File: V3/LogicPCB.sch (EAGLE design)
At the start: 58 parts, among them CON1 CUBE_ORANGE_, CON13 CON-6P-JST-XA, CON14 PINHEAD_1X04-2.54, CON15 CON-4P-JST-XA, CON17 CON-4P-JST-XA, CON18 CON-6P-JST-XA, CON19 USB-TYPE-C-VERT-PROD, CON2 CON-4P-JST-XA, CON20 PINHEAD_1X06-2.54, CON21 CON-4P-JST-XA, CON22 CON-4P-JST-XA, CON23 CON-4P-JST-XA, CON24 CON-4P-JST-XA, CON25 CON-4P-JST-XA, CON26 CON-4P-JST-XA, CON27 CON-4P-JST-XA, CON28 CON-4P-JST-XA, CON29 CON-4P-JST-XA, CON3 PINHEAD_1X08-2.54, CON30 CON-4P-JST-XA, CON32 CON-4P-JST-XA, CON35 CON-12P-JST-XA, CON4 CON-2P-JST-XA, CON5 CON-6P-JST-XA, CON6 CON-4P-JST-XA, CON7 PINHEAD_1X06-2.54, CON8 PINHEAD_1X08-2.54, IC2 AOZ1280, M1 05G_ETHERNET_SWITCH, Q1 IRLML0030

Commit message: updates for V3
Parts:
- removed CON3: PINHEAD_1X08-2.54, pinhead:PINHEAD_1X08-2.54
- added CON9: PINHEAD_1X12-2.54, pinhead:PINHEAD_1X12-2.54
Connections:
- net CAM_RX+ renamed ETH3_TX+
- net CAM_TX+ renamed ETH3_RX+
- net CAM_TX- renamed ETH3_RX-
- net CAN_RX- renamed ETH3_TX-
- net N$10 renamed ETH1_TX+
- net N$11 renamed ETH1_TX-
- net N$12 renamed ETH1_RX+
- net N$17 renamed ETH1_RX-
- net PL_ETH_RX+ renamed ETH5_TX-
- net PL_ETH_RX- renamed ETH5_TX+
- net PL_ETH_TX+ renamed ETH5_RX-
- net PL_ETH_TX- renamed ETH5_RX+
- net 5VFMU: now also CON9.6, CON9.7, CON9.8; no longer CON3.6, CON3.7, CON3.8
- net BATT_CURRENT: now also CON9.1; no longer CON3.1
- net BATT_VOLTAGE: now also CON9.2; no longer CON3.2
- net GND: now also CON35.10, CON9.11, CON9.12, CON9.3, CON9.4, CON9.5; no longer CON3.3, CON3.4, CON3.5
- net SERIAL3_RX: now also CON35.6; no longer CON35.8
- net SERIAL3_TX: now also CON35.5; no longer CON35.7
- net VDD_24V: now also CON35.7, CON35.8; no longer CON35.10
- net VDD_4V: now also CON9.10, CON9.9
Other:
- moved on the sheet: CON13, CON21, CON35, M1G$1, M1J1, M1J3, M1J5

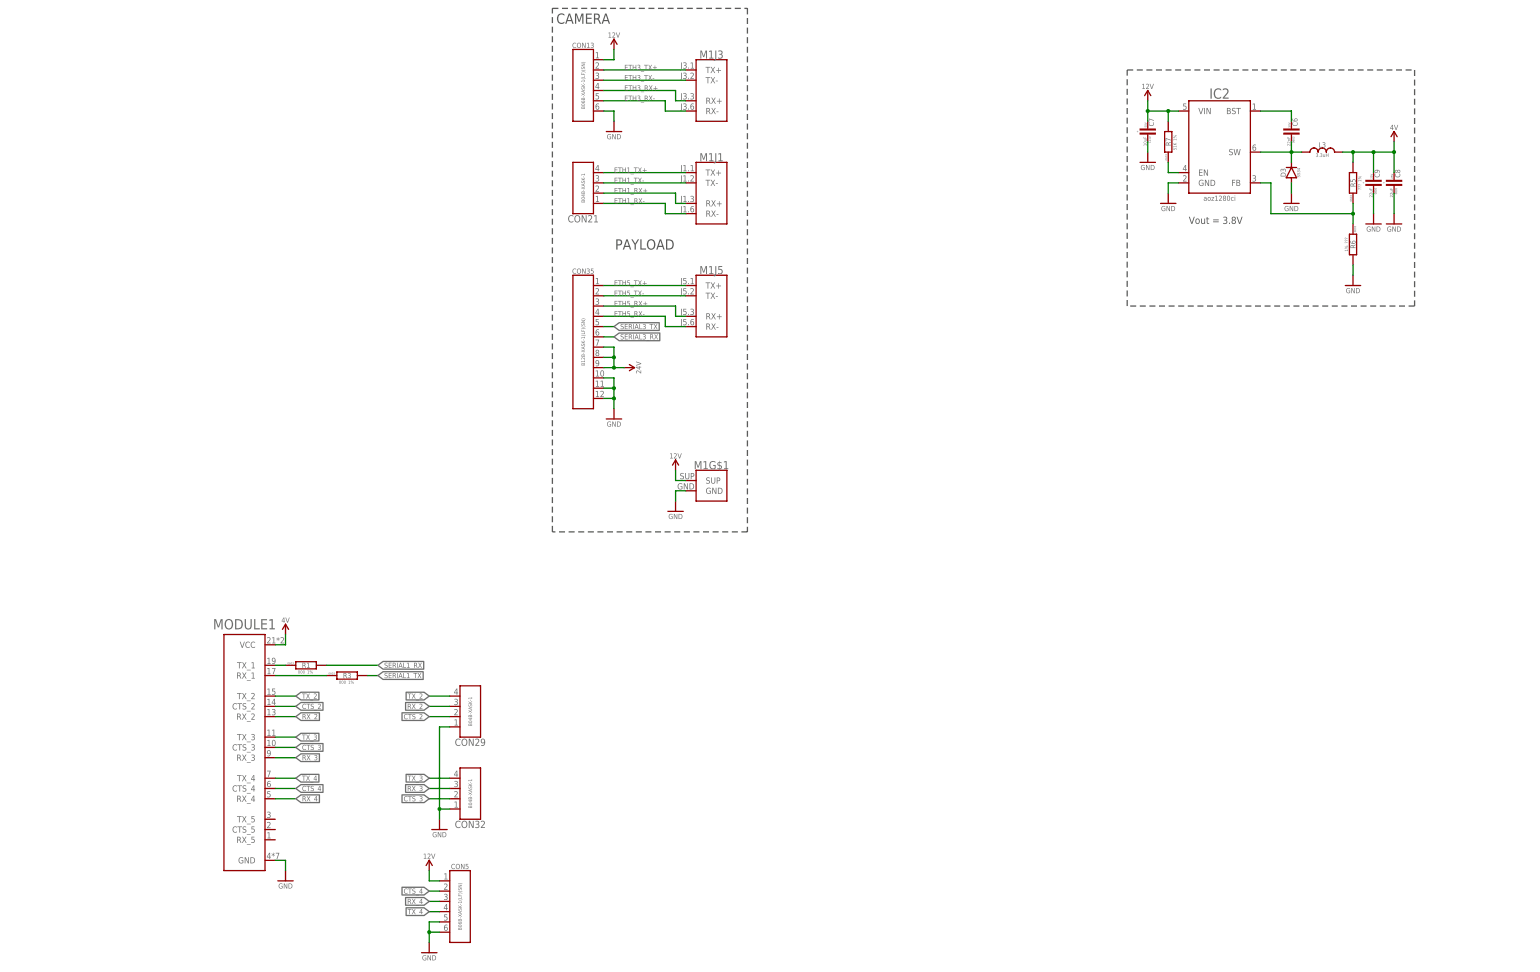
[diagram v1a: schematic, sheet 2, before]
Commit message: silkscreen updates
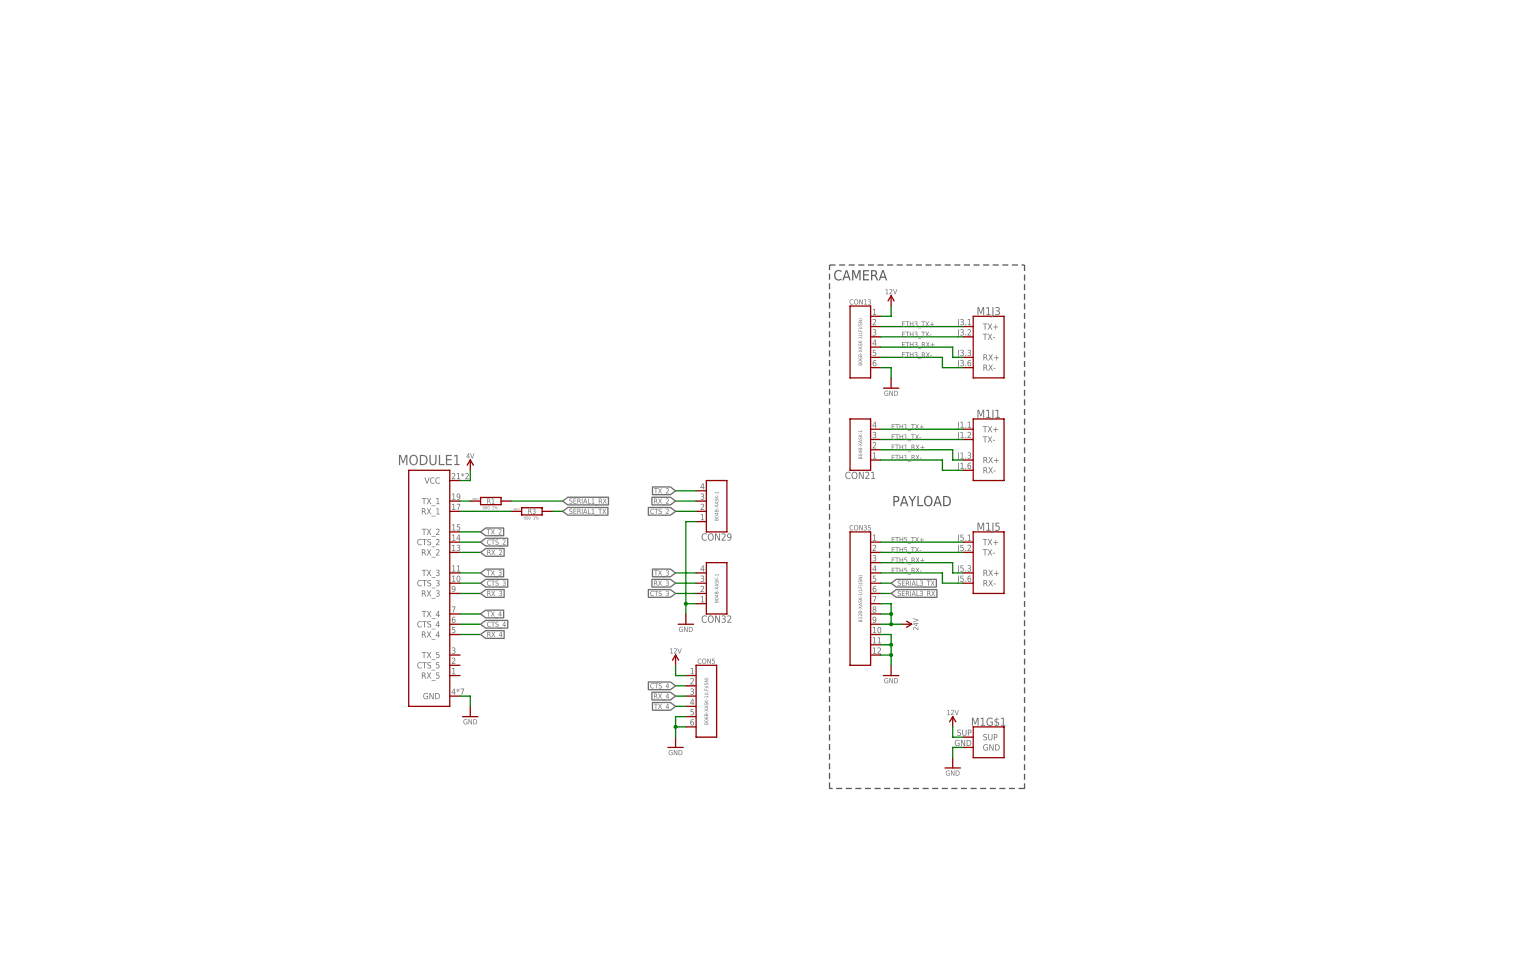
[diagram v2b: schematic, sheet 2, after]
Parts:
- removed C6: 22nF, rc:C-0603
- removed C7: 10uF, rc:C-1210
- removed C8, C9: 22uF, rc:C-0805
- removed D3: SS34, Diodes:SS34
- removed IC2: AOZ1280, dc-dc:AOZ1280
- removed L3: 3.3uH, power_inductors:3.3µH-IHLP-202BZ
- removed R5, R6: ???, rc:R-1%-0603
- removed R7: 51K, rc:R-1%-0603
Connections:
- removed net N$14: C6.2, IC2.BST
- removed net N$15: IC2.FB, R5.1, R6.1
- removed net N$16: IC2.EN, R7.1
- removed net SW2: C6.1, D3.C, IC2.SW, L3.1
- net GND: no longer C7.1, C8.1, C9.1, D3.A, IC2.GND, R6.2
- net VDD_12V: no longer C7.2, IC2.VIN, R7.2
- net VDD_4V: no longer C8.2, C9.2, L3.2, R5.2
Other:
- note removed: "Vout = 3.8V"
- moved on the sheet: CON13, CON21, CON29, CON32, CON35, CON5, M1G$1, M1J1, M1J3, M1J5, MODULE1, R1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

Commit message: V3 finalization
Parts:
- added C4: 10u, rc:C-1206
- added C56: 10n, rc:C-0603
- added C8: 47u, rc:C-1206
- added CON11: CON-4P-JST-XA, Connectors:CON-4P-JST-XA
- added CON3: PINHEAD_1X04-2.54, pinhead:PINHEAD_1X04-2.54
- added D11: SS34, Diodes:SS34
- added IC5: AOZ1280, dc-dc:AOZ1280
- added L1: 3.3uH, power_inductors:3.3µH-IHLP-202BZ
- added M2: 05G_ETHERNET_SWITCH, ali_modules:05G_ETHERNET_SWITCH
- added MODULE2: HLK-7688A, ali_modules:HLK-7688A
- added R30, R32: 51K, rc:R-1%-0603
- added R31: 16K, rc:R-1%-0603
- added T1, T2, T3, T4: H1102NL, misc:H1102NL
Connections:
- new net CAM_RX+: T1.9
- new net CAM_TX+: T1.14
- new net CAM_TX-: T1.16
- new net CAN_RX-: T1.11
- new net HLK_RX0: MODULE2.UART_RXD0
- new net HLK_RX1: MODULE2.UART_RXD1
- new net HLK_TX0: MODULE2.UART_TXD0
- new net HLK_TX1: MODULE2.UART_TXD1
- new net LINK0: MODULE2.EPHY_LED0
- new net LINK1: MODULE2.EPHY_LED1
- new net LINK2: MODULE2.EPHY_LED2
- new net LINK4: MODULE2.EPHY_LED4
- new net LINK_RX+: T4.9
- new net LINK_RX-: T4.11
- new net LINK_TX+: T4.14
- new net LINK_TX-: T4.16
- new net N$88: C56.2, IC5.BST
- new net N$90: IC5.FB, R30.1, R31.1
- new net N$91: IC5.EN, R32.1
- new net P0_RX+: MODULE2.MDI_RP_P0, T2.3
- new net P0_RX-: MODULE2.MDI_RN_P0, T2.1
- new net P0_TX+: MODULE2.MDI_TP_P0, T2.8
- new net P0_TX-: MODULE2.MDI_TN_P0, T2.6
- new net P1_RX+: MODULE2.MDI_RP_P1, T1.8
- new net P1_RX-: MODULE2.MDI_RN_P1, T1.6
- new net P1_TX+: MODULE2.MDI_TP_P1, T1.3
- new net P1_TX-: MODULE2.MDI_TN_P1, T1.1
- new net P2_RX+: MODULE2.MDI_RP_P2, T4.8
- new net P2_RX-: MODULE2.MDI_RN_P2, T4.6
- new net P2_TX+: MODULE2.MDI_TP_P2, T4.3
- new net P2_TX-: MODULE2.MDI_TN_P2, T4.1
- new net P4_RX+: MODULE2.MDI_RP_P4, T3.8
- new net P4_RX-: MODULE2.MDI_RN_P4, T3.6
- new net P4_TX+: MODULE2.MDI_TP_P4, T3.3
- new net P4_TX-: MODULE2.MDI_TN_P4, T3.1
- new net PL_ETH_RX+: T3.11
- new net PL_ETH_RX-: T3.9
- new net PL_ETH_TX+: T3.16
- new net PL_ETH_TX-: T3.14
- new net SW: C56.1, D11.C, IC5.SW, L1.1
- new net USB_DM: CON3.4, MODULE2.USB_DM
- new net USB_DP: CON3.3, MODULE2.USB_DP
- new net VDD_3V3: C8.1, L1.2, MODULE2.3.3V@1, MODULE2.3.3V@2, R30.2
- net GND: now also C4.1, C8.2, CON11.1, CON3.1, D11.A, IC5.GND, MODULE2.GND@1, MODULE2.GND@2, MODULE2.GND@3, MODULE2.GND@4, MODULE2.GND@5, R31.2
- net SERIAL4_RX: now also CON11.4; no longer CON30.4
- net SERIAL4_TX: now also CON11.3; no longer CON30.3
- net SERIAL5_RX: now also CON30.4
- net SERIAL5_TX: now also CON30.3
- net VDD_12V: now also C4.2, CON3.2, IC5.VIN, R32.2
- net VDD_5V: now also CON11.2
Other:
- note added: "CAN2 -> Smart batteries UAVCAN network CAN1 -> GNSS module communication Serial1 -> TELEMETRY Serial2 -> BACKUP Serial3 -> PAYLOAD Serial4 -> BEACON Serial5 -> BACKUP UART"
- note added: "Payload ethernet"
- note added: "Vout = 3.35V"
- note removed: "Backup connectors"
- note removed: "CAN2 -> Smart batteries UAVCAN network CAN1 -> GNSS module communication Serial4 -> BEACON Serial5 -> BACKUP UART Serial1 -> TELEMETRY Serial2 -> PAYLOAD"
- note removed: "Tracking beacon connector"

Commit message: V3 finished
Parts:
- removed C4: 10u, rc:C-1206
- removed C56: 10n, rc:C-0603
- removed C8: 47u, rc:C-1206
- removed CON3: PINHEAD_1X04-2.54, pinhead:PINHEAD_1X04-2.54
- removed D11: SS34, Diodes:SS34
- removed IC5: AOZ1280, dc-dc:AOZ1280
- removed L1: 3.3uH, power_inductors:3.3µH-IHLP-202BZ
- removed M2: 05G_ETHERNET_SWITCH, ali_modules:05G_ETHERNET_SWITCH
- removed MODULE2: HLK-7688A, ali_modules:HLK-7688A
- removed R30, R32: 51K, rc:R-1%-0603
- removed R31: 16K, rc:R-1%-0603
- removed T1, T2, T3, T4: H1102NL, misc:H1102NL
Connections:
- removed net CAM_RX+: T1.9
- removed net CAM_TX+: T1.14
- removed net CAM_TX-: T1.16
- removed net CAN_RX-: T1.11
- removed net HLK_RX0: MODULE2.UART_RXD0
- removed net HLK_RX1: MODULE2.UART_RXD1
- removed net HLK_TX0: MODULE2.UART_TXD0
- removed net HLK_TX1: MODULE2.UART_TXD1
- removed net LINK0: MODULE2.EPHY_LED0
- removed net LINK1: MODULE2.EPHY_LED1
- removed net LINK2: MODULE2.EPHY_LED2
- removed net LINK4: MODULE2.EPHY_LED4
- removed net LINK_RX+: T4.9
- removed net LINK_RX-: T4.11
- removed net LINK_TX+: T4.14
- removed net LINK_TX-: T4.16
- removed net N$88: C56.2, IC5.BST
- removed net N$90: IC5.FB, R30.1, R31.1
- removed net N$91: IC5.EN, R32.1
- removed net P0_RX+: MODULE2.MDI_RP_P0, T2.3
- removed net P0_RX-: MODULE2.MDI_RN_P0, T2.1
- removed net P0_TX+: MODULE2.MDI_TP_P0, T2.8
- removed net P0_TX-: MODULE2.MDI_TN_P0, T2.6
- removed net P1_RX+: MODULE2.MDI_RP_P1, T1.8
- removed net P1_RX-: MODULE2.MDI_RN_P1, T1.6
- removed net P1_TX+: MODULE2.MDI_TP_P1, T1.3
- removed net P1_TX-: MODULE2.MDI_TN_P1, T1.1
- removed net P2_RX+: MODULE2.MDI_RP_P2, T4.8
- removed net P2_RX-: MODULE2.MDI_RN_P2, T4.6
- removed net P2_TX+: MODULE2.MDI_TP_P2, T4.3
- removed net P2_TX-: MODULE2.MDI_TN_P2, T4.1
- removed net P4_RX+: MODULE2.MDI_RP_P4, T3.8
- removed net P4_RX-: MODULE2.MDI_RN_P4, T3.6
- removed net P4_TX+: MODULE2.MDI_TP_P4, T3.3
- removed net P4_TX-: MODULE2.MDI_TN_P4, T3.1
- removed net PL_ETH_RX+: T3.11
- removed net PL_ETH_RX-: T3.9
- removed net PL_ETH_TX+: T3.16
- removed net PL_ETH_TX-: T3.14
- removed net SW: C56.1, D11.C, IC5.SW, L1.1
- removed net USB_DM: CON3.4, MODULE2.USB_DM
- removed net USB_DP: CON3.3, MODULE2.USB_DP
- removed net VDD_3V3: C8.1, L1.2, MODULE2.3.3V@1, MODULE2.3.3V@2, R30.2
- net GND: no longer C4.1, C8.2, CON3.1, D11.A, IC5.GND, MODULE2.GND@1, MODULE2.GND@2, MODULE2.GND@3, MODULE2.GND@4, MODULE2.GND@5, R31.2
- net VDD_12V: no longer C4.2, CON3.2, IC5.VIN, R32.2
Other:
- note removed: "Payload ethernet"
- note removed: "Vout = 3.35V"
